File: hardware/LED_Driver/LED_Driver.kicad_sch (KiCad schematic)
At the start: 11 parts, among them J1 GPIO, J2 Conn_02x11_Counter_Clockwise, U1 CAT24C256

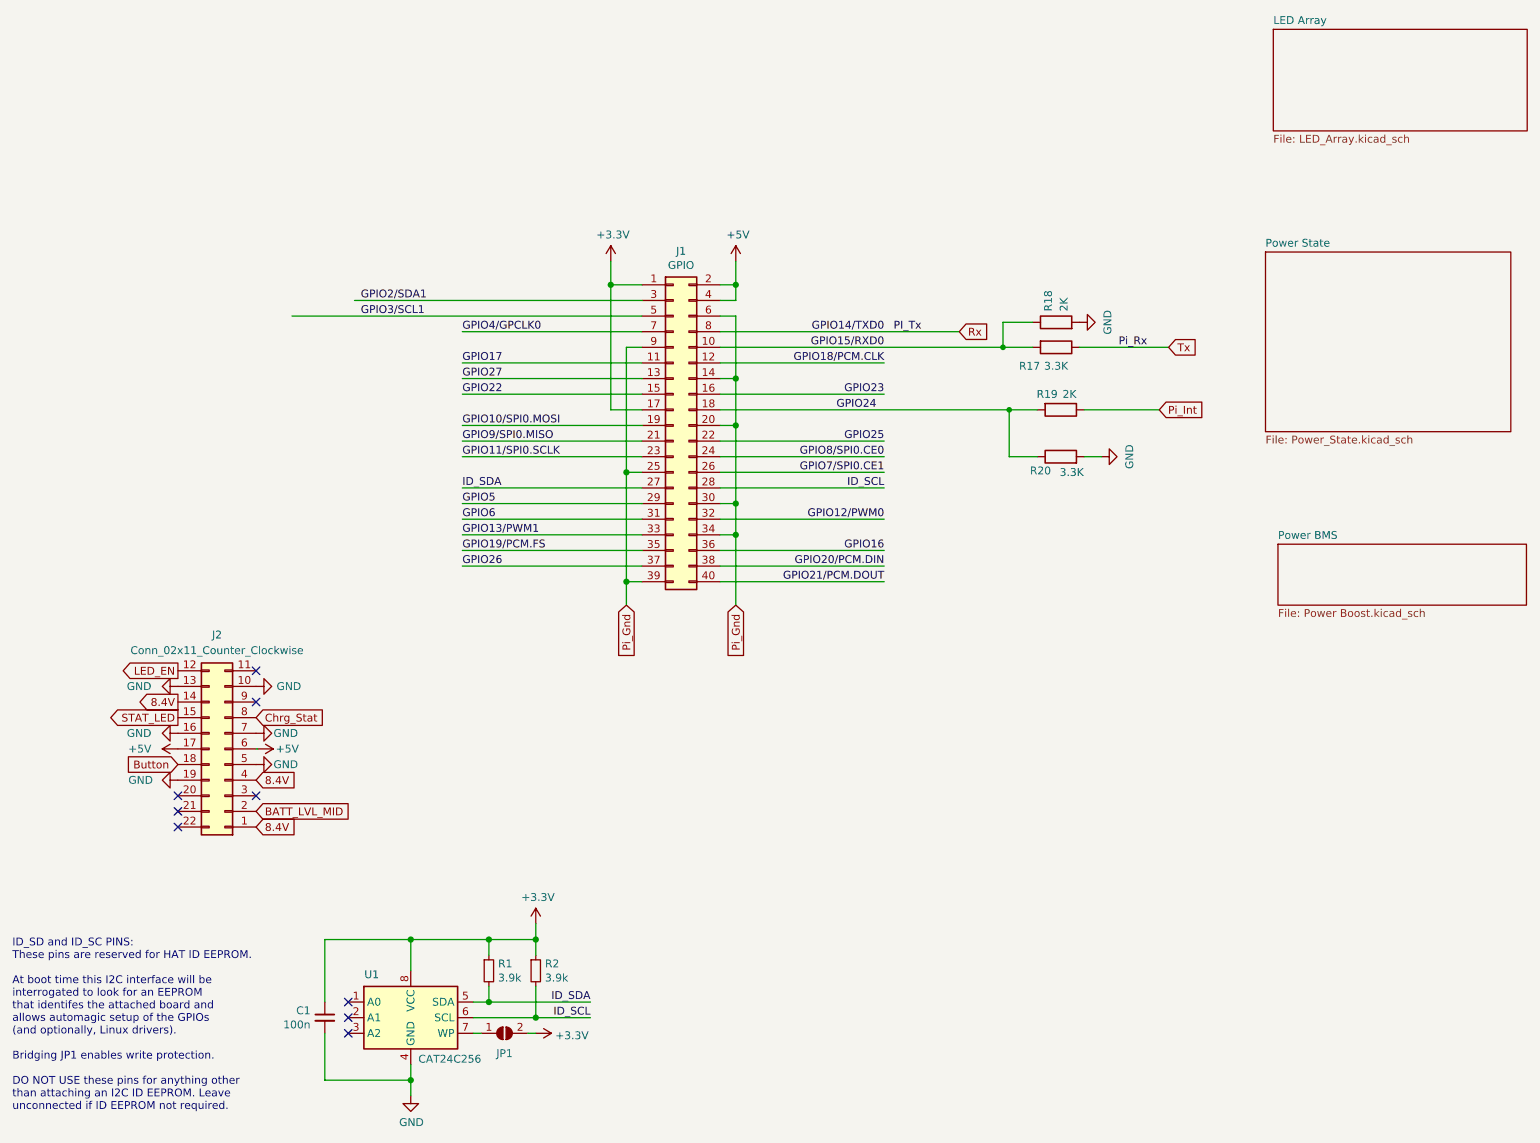
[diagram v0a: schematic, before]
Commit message: Hardware cleanup & enclosure prototype
* Seperates the kicad project into seperate projects per PCB
* initial FreeCAD Assets and prototypes added
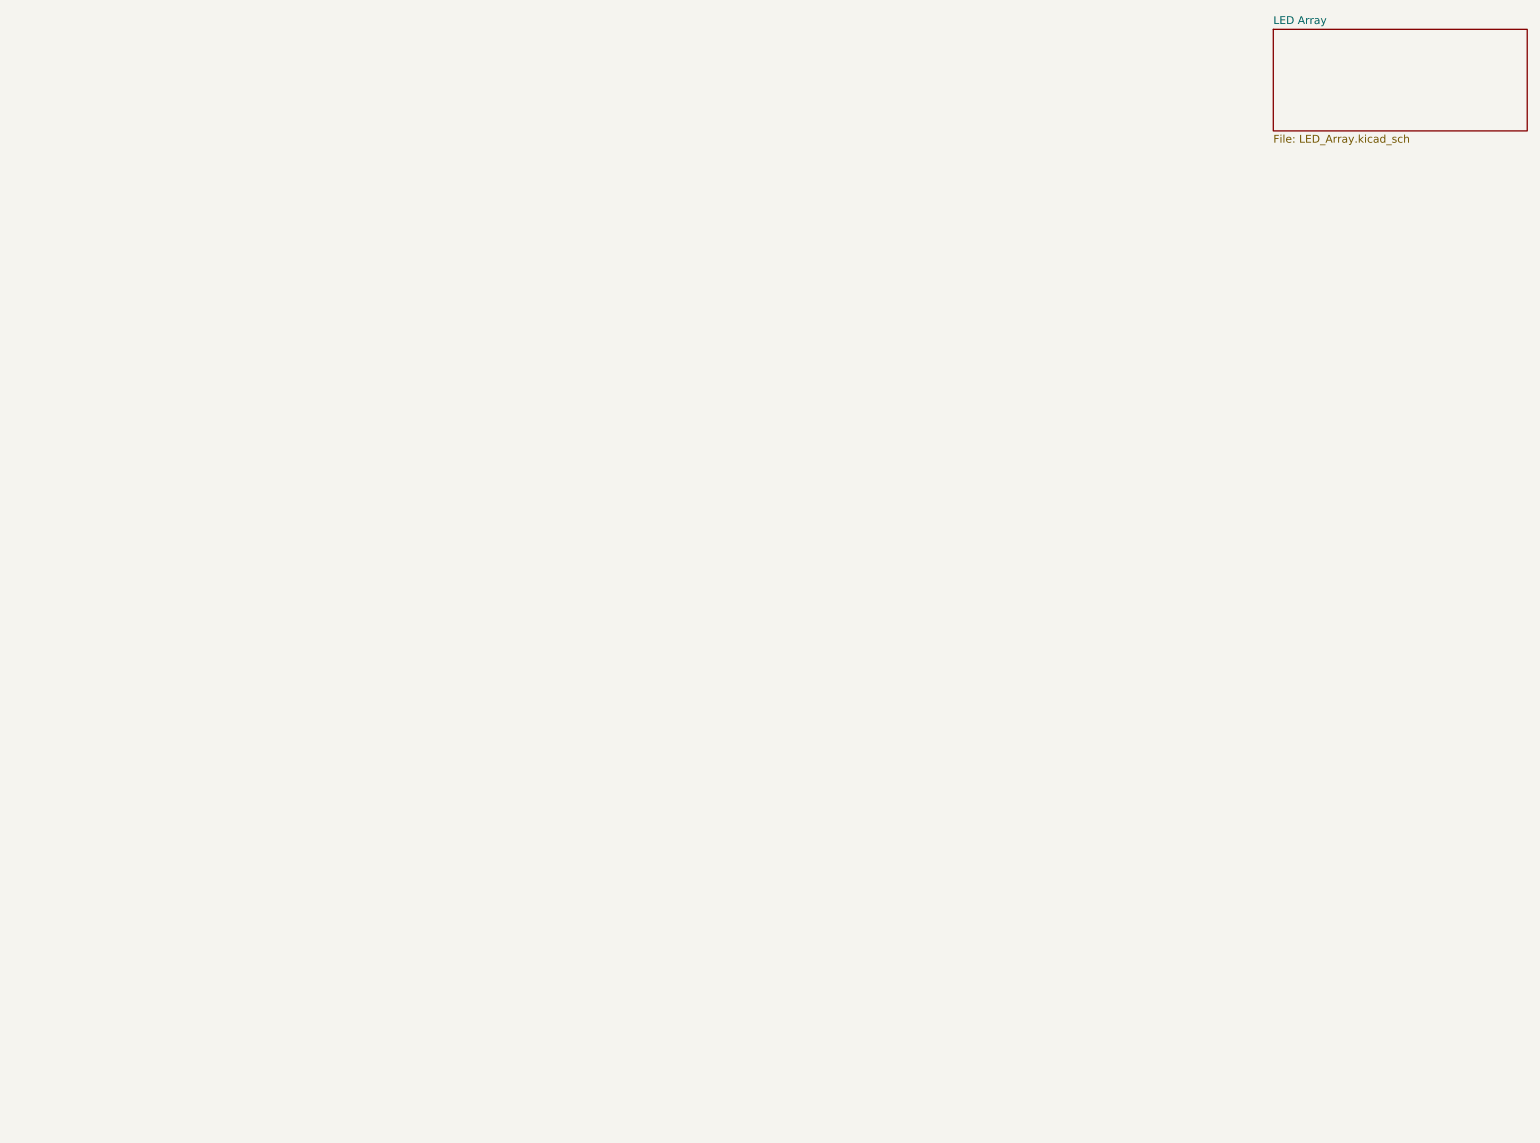
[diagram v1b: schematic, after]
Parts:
- removed C1: 100n, Capacitor_SMD:C_0603_1608Metric_Pad1.08x0.95mm_HandSolder, symbol Device:C_Small
- removed J1: GPIO, Module:Raspberry_Pi_Zero_Socketed_THT_FaceDown_MountingHoles, symbol Connector_Generic:Conn_02x20_Odd_Even
- removed J2: Conn_02x11_Counter_Clockwise, Board:Board_outline, symbol Connector_Generic:Conn_02x11_Counter_Clockwise
- removed JP1: ID_WP, Jumper:SolderJumper-2_P1.3mm_Open_Pad1.0x1.5mm, symbol Jumper:SolderJumper_2_Open
- removed R1, R2: 3.9k, Resistor_SMD:R_0603_1608Metric_Pad0.98x0.95mm_HandSolder, symbol Device:R_Small
- removed R17, R20: 3.3K, Resistor_SMD:R_0603_1608Metric_Pad0.98x0.95mm_HandSolder, symbol Device:R
- removed R18, R19: 2K, Resistor_SMD:R_0603_1608Metric_Pad0.98x0.95mm_HandSolder, symbol Device:R
- removed U1: CAT24C256, CAT24C256WI-GT3:SOIC127P600X175-8N, symbol Memory_EEPROM:CAT24C256
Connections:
- no-connect marks 9 -> 0
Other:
- removed sheet Power BMS
- removed sheet Power State
- note removed: "ID_SD and ID_SC PINS: These pins are reserved for HAT ID EEPROM. At boot time this I2C interface will be interrogated to look for an EEPROM that identifes the attached board and allows automagic setup of the GPIOs (and optionally, Linux drivers). Bridging JP1 enables write protection. DO NOT USE these pins for anything other than attaching an I2C ID EEPROM. Leave unconnected if ID EEPROM not requ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"
